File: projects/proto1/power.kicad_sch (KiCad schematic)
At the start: 10 parts, among them J10 SMC_UART, J9 ATX-24, U19 74LS00, U25 SYS_Header, U26 74LS04, U27 ATmega32-16P

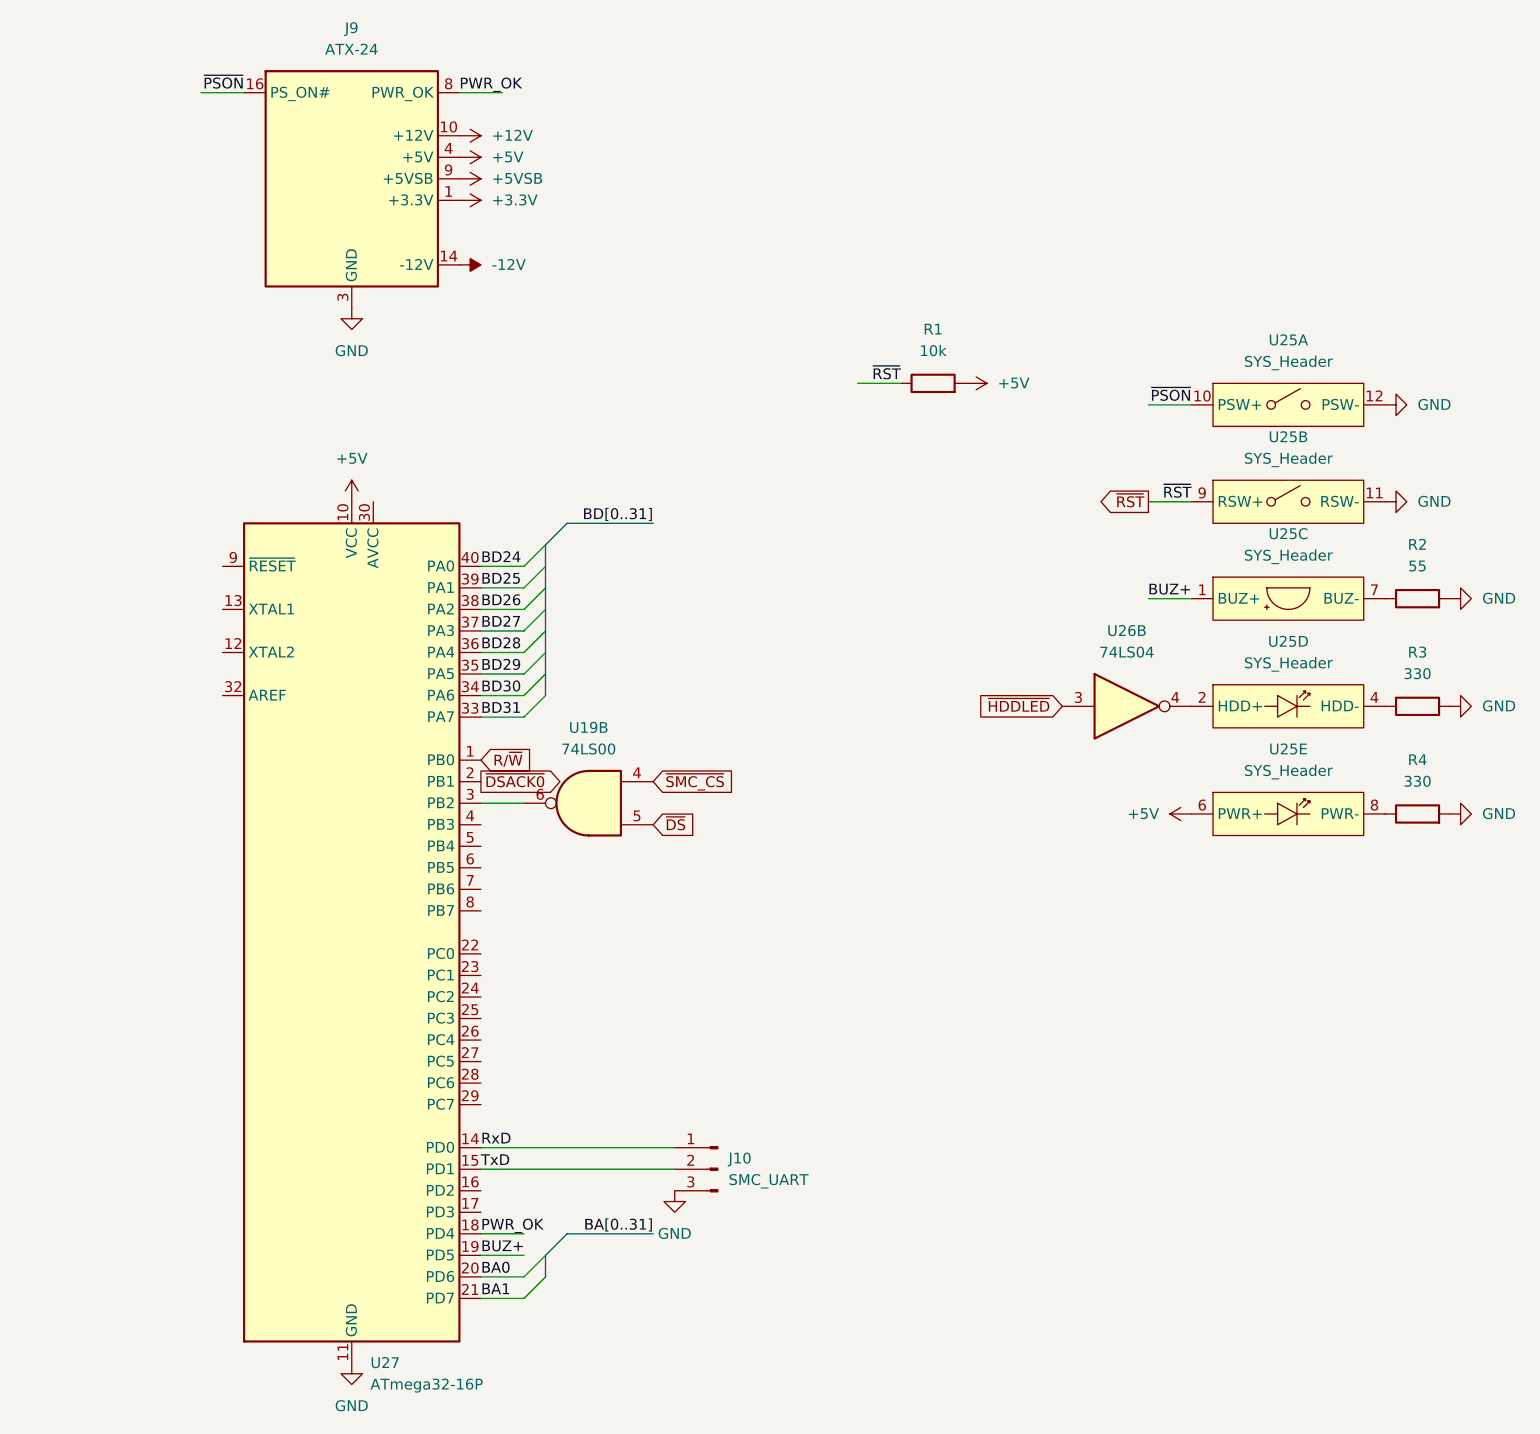
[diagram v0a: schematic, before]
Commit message: Renamed CMC to SCU, changed verification method to cocotb, and modified pcb schematic
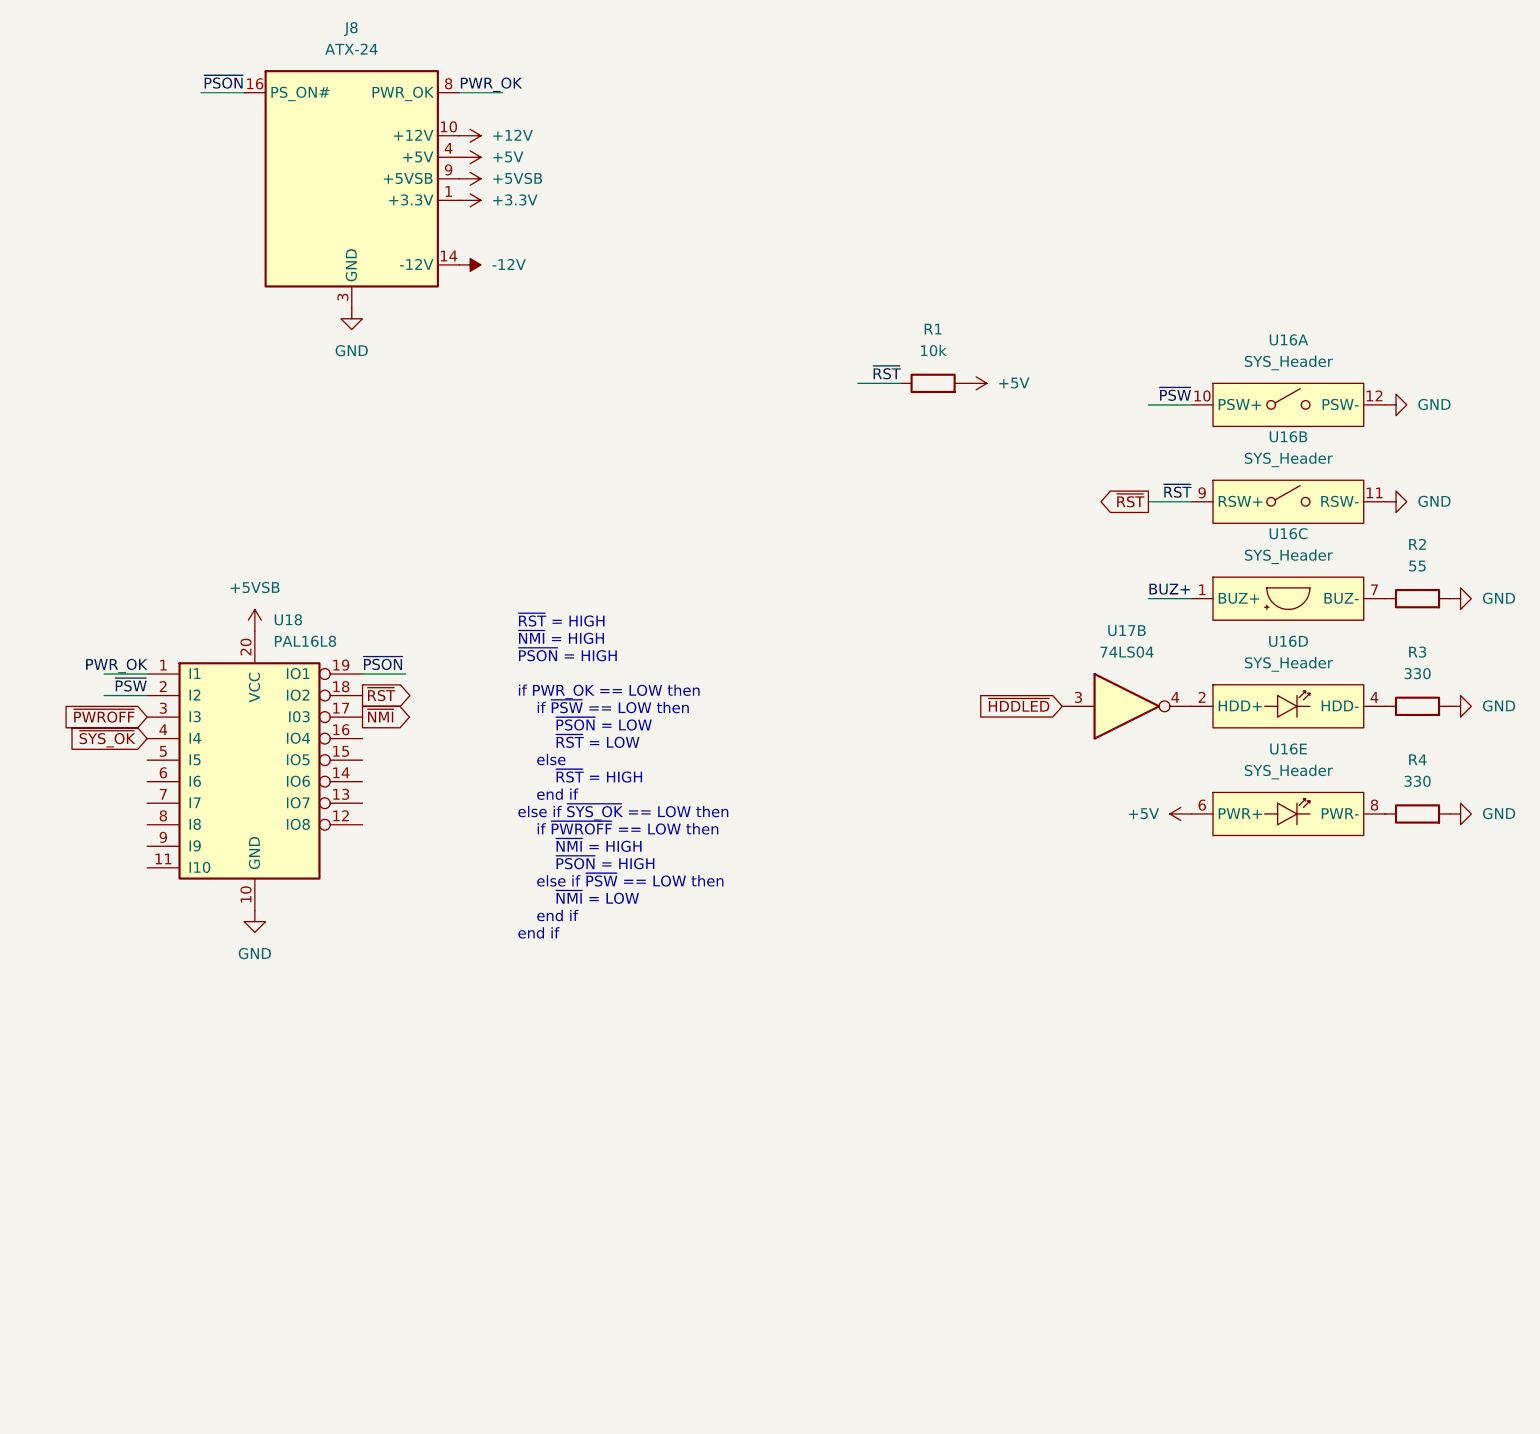
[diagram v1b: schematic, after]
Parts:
- removed J10: SMC_UART, Connector_PinHeader_2.54mm:PinHeader_1x03_P2.54mm_Vertical, symbol Connector:Conn_01x03_Pin
- removed U19: 74LS00, Package_DIP:DIP-14_W7.62mm_Socket, symbol 74xx:74LS00
- removed U27: ATmega32-16P, Package_DIP:DIP-40_W15.24mm_Socket, symbol MCU_Microchip_ATmega:ATmega32-16P
- added U18: PAL16L8, symbol Logic_Programmable:PAL16L8
- renumbered J9 to J8, U25 to U16, U26 to U17
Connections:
- net +5VSB: now also U18.20 (VCC)
- net GND: now also U18.10 (GND)
- net PWR_OK: now also U18.1 (I1)
- net ~{PSON}: now also U18.19 (IO1); no longer U16.10 (PSW+)
- net ~{RST}: now also U18.18 (IO2)
- new net ~{NMI}: U18.17 (I03)
- new net ~{PSW}: U16.10 (PSW+), U18.2 (I2)
- new net ~{PWROFF}: U18.3 (I3)
- new net ~{SYS_OK}: U18.4 (I4)
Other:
- note added: "~{RST} = HIGH ~{NMI} = HIGH ~{PSON} = HIGH if PWR_OK == LOW then if ~{PSW} == LOW then ~{PSON} = LOW ~{RST} = LOW else ~{RST} = HIGH end if else if ~{SYS_OK} == LOW then if ~{PWROFF} == LOW then ~{NMI} = HIGH ~{PSON} = HIGH else if ~{PSW} == LOW then ~{NMI} = LOW end if end if"
